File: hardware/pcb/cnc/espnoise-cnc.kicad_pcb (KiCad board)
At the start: 2 copper layers, 70 x 50 mm, 18 parts, among them J1 USB-C 5V JST XH 1x2, J2 CONTROLLER JST XH 1x10, J3 LED STRIP JST XH 1x5, Q1 2N3904, SW1 MUTE (7-7 WS), SW2 BUZZER ENABLE (7-7 ZS), U1 SN74AHCT125N

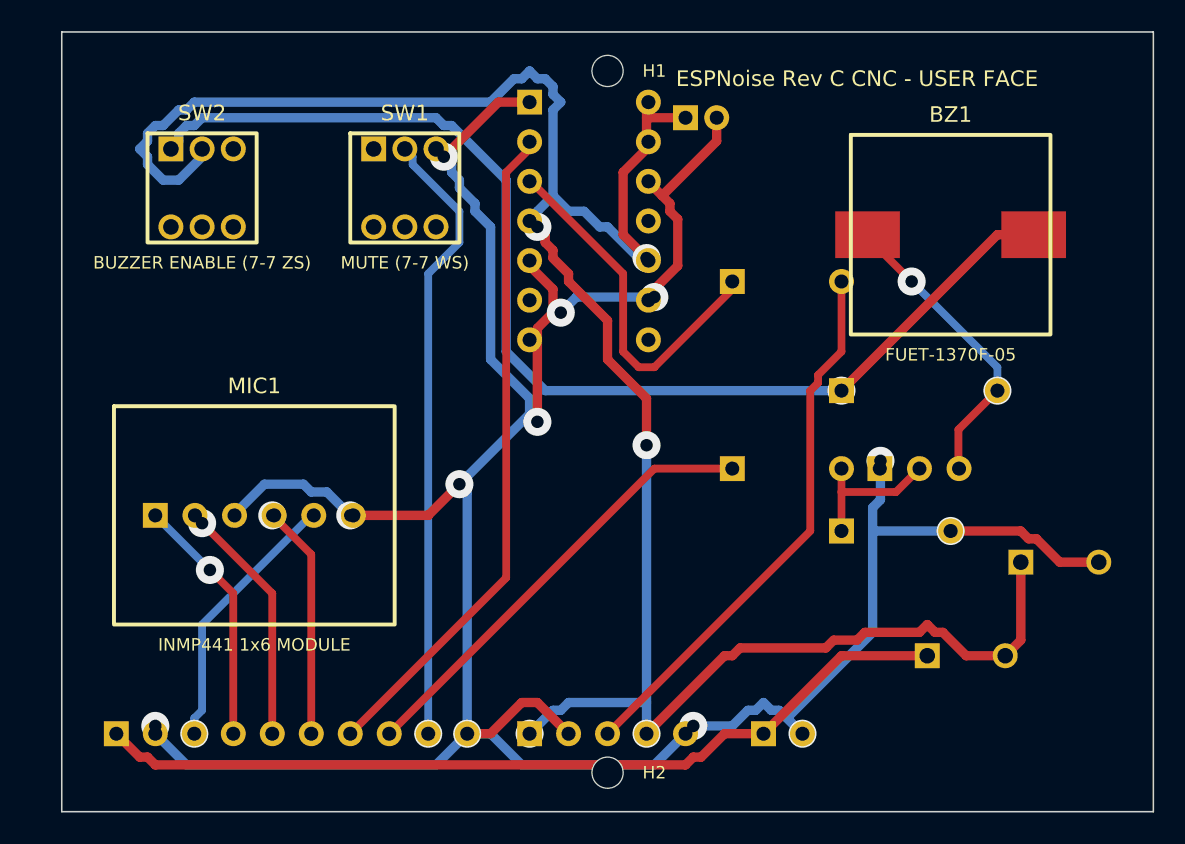
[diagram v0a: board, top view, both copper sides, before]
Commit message: Fit two lean CNC PCBs on one panel
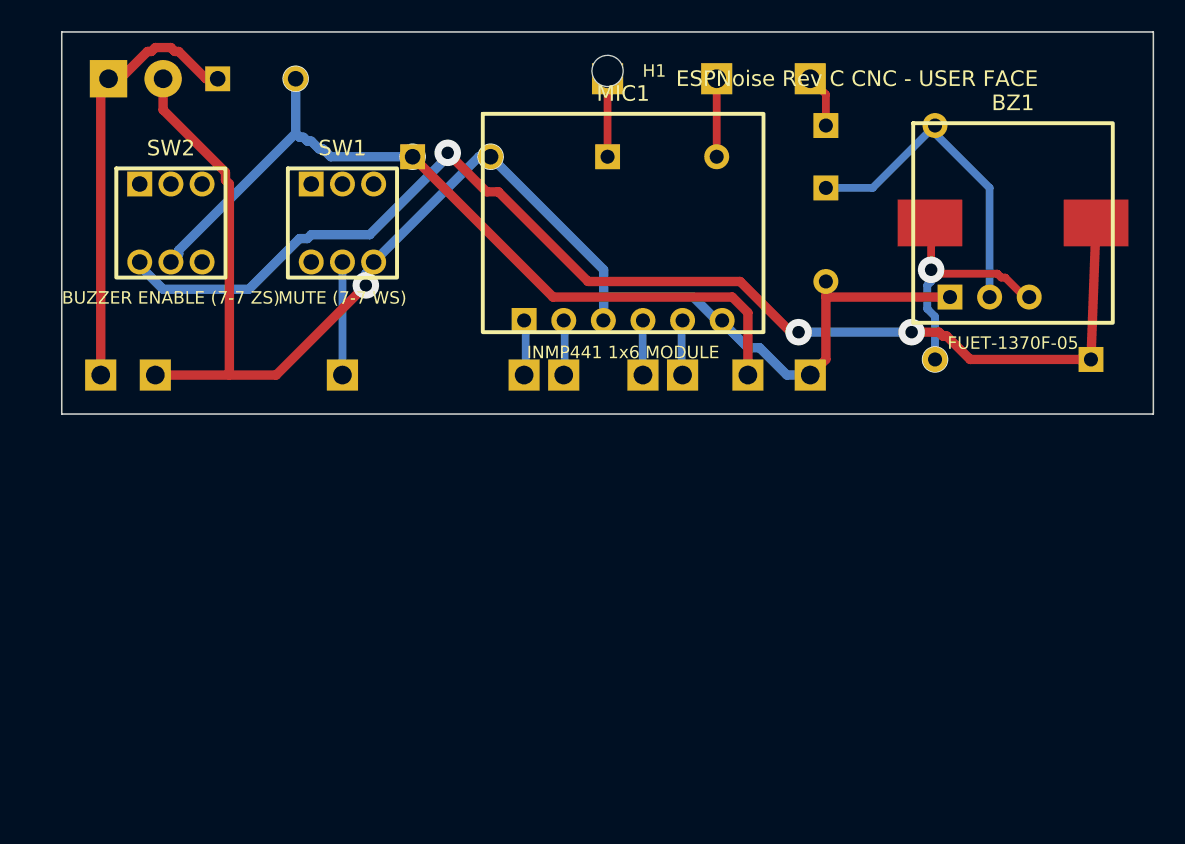
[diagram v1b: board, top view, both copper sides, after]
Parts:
- removed C1: 100nF, THT:C_Disc_P2.00mm
- removed H2: , Mechanical:RegistrationHole_2mm
- removed J1: USB-C 5V JST XH 1x2, JST:B2B-XH-A
- removed J2: CONTROLLER JST XH 1x10, JST:B10B-XH-A
- removed J3: LED STRIP JST XH 1x5, JST:B5B-XH-A
- removed U1: SN74AHCT125N, Package_DIP:DIP-14_W7.62mm
- added P1: 5 V POWER WIRES, ESPNoise:WirePads_2_P3.5mm, B.Cu at (0.00, 0.00)
- added W1: ESP32 +5V, ESPNoise:WireTerminal_D2.0mm, B.Cu at (0.00, 0.00)
- added W10: LED +5V, ESPNoise:WireTerminal_D2.0mm, B.Cu at (0.00, 0.00)
- added W11: LED DATA, ESPNoise:WireTerminal_D2.0mm, B.Cu at (0.00, 0.00)
- added W12: LED GND, ESPNoise:WireTerminal_D2.0mm, B.Cu at (0.00, 0.00)
- added W2: ESP32 GND, ESPNoise:WireTerminal_D2.0mm, B.Cu at (0.00, 0.00)
- added W3: ESP32 MUTE, ESPNoise:WireTerminal_D2.0mm, B.Cu at (0.00, 0.00)
- added W4: ESP32 MIC SCK, ESPNoise:WireTerminal_D2.0mm, B.Cu at (0.00, 0.00)
- added W5: ESP32 MIC WS, ESPNoise:WireTerminal_D2.0mm, B.Cu at (0.00, 0.00)
- added W6: ESP32 MIC SD, ESPNoise:WireTerminal_D2.0mm, B.Cu at (0.00, 0.00)
- added W7: ESP32 3V3, ESPNoise:WireTerminal_D2.0mm, B.Cu at (0.00, 0.00)
- added W8: ESP32 LED DATA, ESPNoise:WireTerminal_D2.0mm, B.Cu at (0.00, 0.00)
- added W9: ESP32 BUZZER, ESPNoise:WireTerminal_D2.0mm, B.Cu at (0.00, 0.00)
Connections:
- R1 pad 1: LED_DATA_5V_RAW -> LED_DATA_3V3
- R1 pad 2: LED_DATA_5V -> LED_DATA
- SW1 pad 2: MUTE_N -> (no net)
- SW1 pad 3: GND -> (no net)
- SW1 pad 5: (no net) -> MUTE_N
- SW1 pad 6: (no net) -> GND
- SW2 pad 1: +5V_BUZZER_SW -> (no net)
- SW2 pad 2: +5V_PERIPH -> (no net)
- SW2 pad 4: (no net) -> +5V_BUZZER_SW
- SW2 pad 5: (no net) -> +5V_PERIPH
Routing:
- net GND: track 192.7 -> 91.9 mm, vias 12 -> 3
- net +5V_PERIPH: track 144.3 -> 52.8 mm, vias 5 -> 2
- net LED_DATA_3V3: track 42.8 -> 5.00 mm
- net LED_DATA_5V: track 35.2 -> 0.00 mm
- net MUTE_N: track 39.8 -> 7.25 mm
- net +5V_IN: track 55.7 -> 27.9 mm
- net BUZZER_PWM: track 29.0 -> 3.41 mm
- net LED_DATA_5V_RAW: track 23.5 -> 0.00 mm
- net +3V3: track 17.1 -> 3.50 mm
- net MIC_WS: track 16.1 -> 3.50 mm
- net MIC_SCK: track 16.1 -> 3.50 mm
- net MIC_SD: track 15.0 -> 3.50 mm
- net BUZZER_BASE: track 9.62 -> 21.0 mm
- net +5V_BUZZER_SW: track 74.5 -> 79.9 mm, vias 1 -> 3
- net LED_DATA: track 0.00 -> 5.00 mm
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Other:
- board size 70 x 50 mm -> 70 x 24.5 mm
- board text added: "INTERNAL - SOLDER WIRE VIAS BOTH FACES"
- board text removed: "INTERNAL FACE - WIRE VIAS: SOLDER BOTH FACES"

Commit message: Correct CNC microphone and buzzer footprints
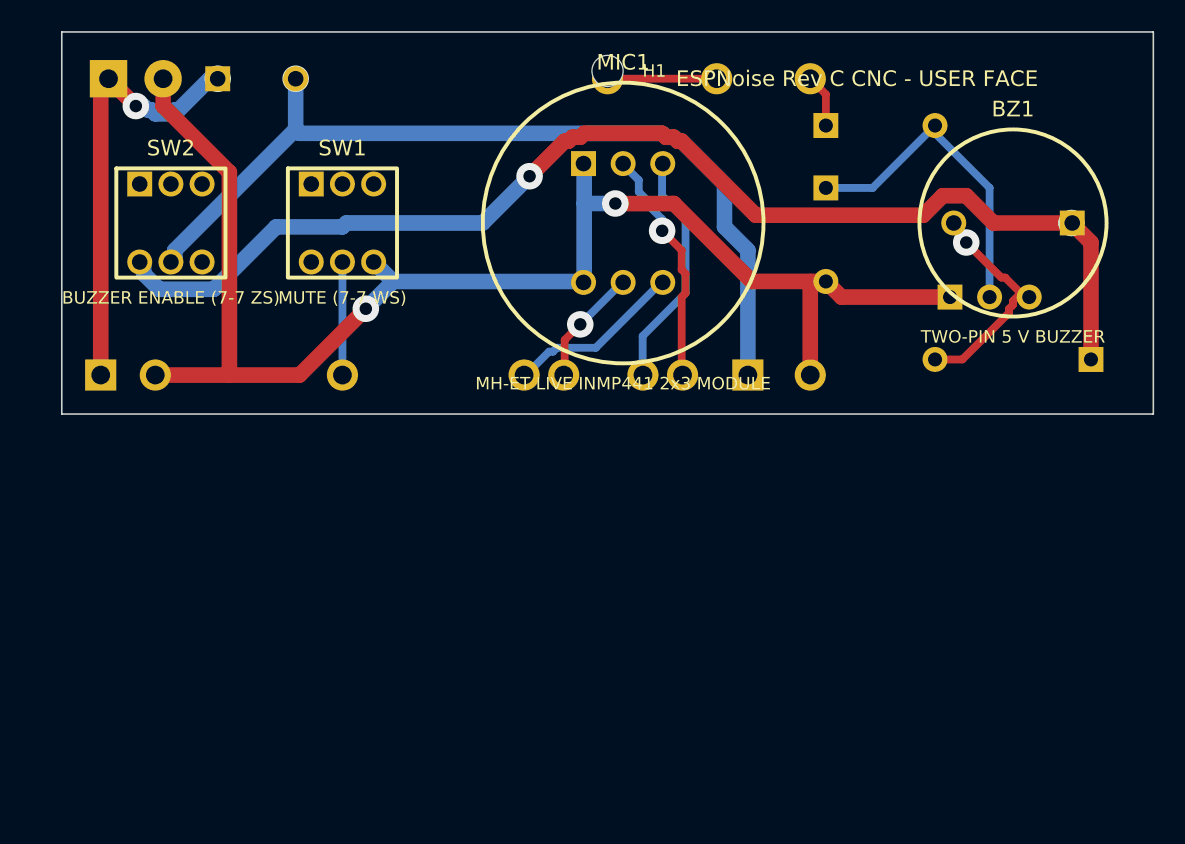
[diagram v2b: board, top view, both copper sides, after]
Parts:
- removed C2: 1000uF 10V, THT:CP_Radial_D8_P5.00mm
- removed P1: 5 V POWER WIRES, ESPNoise:WirePads_2_P3.5mm
- removed R1: 330R, THT:Axial
- removed W1: ESP32 +5V, ESPNoise:WireTerminal_D2.0mm
- removed W10: LED +5V, ESPNoise:WireTerminal_D2.0mm
- removed W11: LED DATA, ESPNoise:WireTerminal_D2.0mm
- removed W12: LED GND, ESPNoise:WireTerminal_D2.0mm
- removed W2: ESP32 GND, ESPNoise:WireTerminal_D2.0mm
- removed W3: ESP32 MUTE, ESPNoise:WireTerminal_D2.0mm
- removed W4: ESP32 MIC SCK, ESPNoise:WireTerminal_D2.0mm
- removed W5: ESP32 MIC WS, ESPNoise:WireTerminal_D2.0mm
- removed W6: ESP32 MIC SD, ESPNoise:WireTerminal_D2.0mm
- removed W7: ESP32 3V3, ESPNoise:WireTerminal_D2.0mm
- removed W8: ESP32 LED DATA, ESPNoise:WireTerminal_D2.0mm
- removed W9: ESP32 BUZZER, ESPNoise:WireTerminal_D2.0mm
- added J_ESP32: ESP32 INDIVIDUAL WIRES, ESPNoise:IndividualWireGroup_ESP32, B.Cu at (0.00, 0.00)
- added J_LED: LED STRIP INDIVIDUAL WIRES, ESPNoise:IndividualWireGroup_LED, B.Cu at (0.00, 0.00)
- added PWR1: 5 V POWER WIRES, ESPNoise:WirePads_2_P3.5mm, B.Cu at (0.00, 0.00)
- BZ1: value FUET-1370F-05 -> TWO-PIN 5 V BUZZER; footprint ESPNoise:FUET-1370F-05 -> ESPNoise:Buzzer_THT_2Pin_P7.60mm_D12mm
- MIC1: value INMP441 1x6 MODULE -> MH-ET LIVE INMP441 2x3 MODULE; footprint ESPNoise:INMP441_1x6_P2.54mm -> ESPNoise:MH_ET_LIVE_INMP441_2x3_P2.54_Row7.62
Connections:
- MIC1 pad 1: MIC_SCK -> GND
- MIC1 pad 2: MIC_WS -> +3V3
- MIC1 pad 3: GND -> MIC_SD
- MIC1 pad 4: MIC_SD -> GND
- MIC1 pad 5: +3V3 -> MIC_WS
- MIC1 pad 6: GND -> MIC_SCK
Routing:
- net +3V3: track 3.50 -> 15.3 mm
- net MIC_SD: track 3.50 -> 15.3 mm
- net MIC_SCK: track 3.50 -> 11.2 mm
- net LED_DATA_3V3: track 5.00 -> 0.00 mm
- net +5V_PERIPH: track 52.8 -> 56.9 mm
- net MIC_WS: track 3.50 -> 7.55 mm
- net +5V_BUZZER_SW: track 79.9 -> 77.6 mm, vias 3 -> 2
- net LED_DATA: track 5.00 -> 7.00 mm
- net BUZZER_COLLECTOR: track 16.0 -> 14.6 mm, vias 2 -> 1
- net +5V_IN: track 27.9 -> 28.1 mm, vias 0 -> 2
- net GND: track 91.9 -> 92.0 mm, vias 3 -> 2

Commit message: Apply measured CNC part dimensions
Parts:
- BZ1: footprint ESPNoise:Buzzer_THT_2Pin_P7.60mm_D12mm -> ESPNoise:Buzzer_THT_2Pin_P6.50mm_D12mm
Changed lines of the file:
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@@
     (layer "F.Cu")
     (at 0 0)
-    (property "Reference" "MIC1" (at 36.000 1.950 0) (layer "F.SilkS") (effects (font (size 1 1) (thickness 0.15))))
-    (property "Value" "MH-ET LIVE INMP441 2x3 MODULE" (at 36.000 22.550 0) (layer "F.SilkS") (effects (font (size 0.8 0.8) (thickness 0.12))))
-    (fp_circle (center 36.000 12.250) (end 45.000 12.250) (stroke (width 0.25) (type default)) (fill none) (layer "F.SilkS"))
+    (property "Reference" "MIC1" (at 36.000 4.450 0) (layer "F.SilkS") (effects (font (size 1 1) (thickness 0.15))))
+    (property "Value" "MH-ET LIVE INMP441 2x3 MODULE" (at 36.000 20.050 0) (layer "F.SilkS") (effects (font (size 0.8 0.8) (thickness 0.12))))
+    (fp_circle (center 36.000 12.250) (end 42.500 12.250) (stroke (width 0.25) (type default)) (fill none) (layer "F.SilkS"))
     (pad "1" thru_hole rect (at 33.460 8.440) (size 1.600 1.600) (drill 1.000) (layers "*.Cu" "*.Mask") (net 8 "GND"))
     (pad "2" thru_hole circle (at 36.000 8.440) (size 1.600 1.600) (drill 1.000) (layers "*.Cu" "*.Mask") (net 1 "+3V3"))
@@
     (pad "6" thru_hole circle (at 38.540 16.060) (size 1.600 1.600) (drill 1.000) (layers "*.Cu" "*.Mask") (net 10 "MIC_SCK"))
   )
-  (footprint "ESPNoise:Buzzer_THT_2Pin_P7.60mm_D12mm"
+  (footprint "ESPNoise:Buzzer_THT_2Pin_P6.50mm_D12mm"
     (layer "F.Cu")
     (at 0 0)
@@
     (property "Value" "TWO-PIN 5 V BUZZER" (at 61.000 19.550 0) (layer "F.SilkS") (effects (font (size 0.8 0.8) (thickness 0.12))))
     (fp_circle (center 61.000 12.250) (end 67.000 12.250) (stroke (width 0.25) (type default)) (fill none) (layer "F.SilkS"))
-    (pad "1" thru_hole rect (at 64.800 12.250) (size 1.600 1.600) (drill 1.000) (layers "*.Cu" "*.Mask") (net 2 "+5V_BUZZER_SW"))
-    (pad "2" thru_hole circle (at 57.200 12.250) (size 1.600 1.600) (drill 1.000) (layers "*.Cu" "*.Mask") (net 6 "BUZZER_COLLECTOR"))
+    (pad "1" thru_hole rect (at 64.250 12.250) (size 1.600 1.600) (drill 0.800) (layers "*.Cu" "*.Mask") (net 2 "+5V_BUZZER_SW"))
+    (pad "2" thru_hole circle (at 57.750 12.250) (size 1.600 1.600) (drill 0.800) (layers "*.Cu" "*.Mask") (net 6 "BUZZER_COLLECTOR"))
   )
   (footprint "ESPNoise:WirePads_2_P3.5mm"
@@
   (segment (start 55.750 6.250) (end 59.500 10.000) (width 0.500) (layer "B.Cu") (net 5))
   (segment (start 59.500 10.000) (end 59.500 17.000) (width 0.500) (layer "B.Cu") (net 5))
-  (segment (start 57.250 12.250) (end 57.500 12.500) (width 0.500) (layer "B.Cu") (net 6))
-  (segment (start 57.500 12.500) (end 57.500 12.750) (width 0.500) (layer "B.Cu") (net 6))
-  (segment (start 57.500 12.750) (end 57.750 13.000) (width 0.500) (layer "B.Cu") (net 6))
-  (segment (start 57.750 13.000) (end 57.750 13.250) (width 0.500) (layer "B.Cu") (net 6))
-  (segment (start 57.750 13.250) (end 58.000 13.500) (width 0.500) (layer "B.Cu") (net 6))
-  (segment (start 58.000 13.500) (end 60.250 15.750) (width 0.500) (layer "F.Cu") (net 6))
-  (segment (start 60.250 15.750) (end 60.500 15.750) (width 0.500) (layer "F.Cu") (net 6))
-  (segment (start 60.500 15.750) (end 61.750 17.000) (width 0.500) (layer "F.Cu") (net 6))
-  (segment (start 61.750 17.000) (end 62.000 17.000) (width 0.500) (layer "F.Cu") (net 6))
-  (segment (start 61.500 16.750) (end 61.000 17.250) (width 0.500) (layer "F.Cu") (net 6))
-  (segment (start 61.000 17.250) (end 61.000 17.500) (width 0.500) (layer "F.Cu") (net 6))
-  (segment (start 61.000 17.500) (end 60.750 17.750) (width 0.500) (layer "F.Cu") (net 6))
-  (segment (start 60.750 17.750) (end 60.750 18.000) (width 0.500) (layer "F.Cu") (net 6))
-  (segment (start 60.750 18.000) (end 57.750 21.000) (width 0.500) (layer "F.Cu") (net 6))
-  (segment (start 57.750 21.000) (end 56.000 21.000) (width 0.500) (layer "F.Cu") (net 6))
+  (segment (start 57.750 12.250) (end 58.000 12.500) (width 0.500) (layer "B.Cu") (net 6))
+  (segment (start 58.000 12.500) (end 62.000 16.500) (width 0.500) (layer "F.Cu") (net 6))
+  (segment (start 62.000 16.500) (end 62.000 17.000) (width 0.500) (layer "F.Cu") (net 6))
+  (segment (start 62.000 17.000) (end 58.000 21.000) (width 0.500) (layer "F.Cu") (net 6))
+  (segment (start 58.000 21.000) (end 56.000 21.000) (width 0.500) (layer "F.Cu") (net 6))
   (segment (start 5.000 14.750) (end 5.250 15.000) (width 1.000) (layer "B.Cu") (net 2))
   (segment (start 5.250 15.000) (end 5.250 15.500) (width 1.000) (layer "B.Cu") (net 2))
@@
   (segment (start 39.500 7.000) (end 39.750 7.000) (width 1.000) (layer "F.Cu") (net 2))
   (segment (start 39.750 7.000) (end 44.500 11.750) (width 1.000) (layer "F.Cu") (net 2))
-  (segment (start 44.500 11.750) (end 55.250 11.750) (width 1.000) (layer "F.Cu") (net 2))
-  (segment (start 55.250 11.750) (end 56.500 10.500) (width 1.000) (layer "F.Cu") (net 2))
-  (segment (start 56.500 10.500) (end 58.000 10.500) (width 1.000) (layer "F.Cu") (net 2))
-  (segment (start 58.000 10.500) (end 59.750 12.250) (width 1.000) (layer "F.Cu") (net 2))
-  (segment (start 59.750 12.250) (end 64.750 12.250) (width 1.000) (layer "F.Cu") (net 2))
-  (segment (start 64.750 12.250) (end 66.000 13.500) (width 1.000) (layer "F.Cu") (net 2))
-  (segment (start 66.000 13.500) (end 66.000 21.000) (width 1.000) (layer "F.Cu") (net 2))
+  (segment (start 44.500 11.750) (end 55.750 11.750) (width 1.000) (layer "F.Cu") (net 2))
+  (segment (start 55.750 11.750) (end 57.000 10.500) (width 1.000) (layer "F.Cu") (net 2))
+  (segment (start 57.000 10.500) (end 58.500 10.500) (width 1.000) (layer "F.Cu") (net 2))
+  (segment (start 58.500 10.500) (end 60.250 12.250) (width 1.000) (layer "F.Cu") (net 2))
+  (segment (start 60.250 12.250) (end 64.250 12.250) (width 1.000) (layer "F.Cu") (net 2))
+  (segment (start 64.250 12.250) (end 66.000 14.000) (width 1.000) (layer "F.Cu") (net 2))
+  (segment (start 66.000 14.000) (end 66.000 21.000) (width 1.000) (layer "F.Cu") (net 2))
   (via (at 29.750 22.000) (size 1.700) (drill 0.800) (layers "F.Cu" "B.Cu") (net 10))
   (via (at 33.250 18.750) (size 1.700) (drill 0.800) (layers "F.Cu" "B.Cu") (net 12))
@@
   (via (at 15.000 3.000) (size 1.700) (drill 0.800) (layers "F.Cu" "B.Cu") (net 4))
   (via (at 44.000 22.000) (size 1.700) (drill 0.800) (layers "F.Cu" "B.Cu") (net 4))
-  (via (at 58.000 13.500) (size 1.700) (drill 0.800) (layers "F.Cu" "B.Cu") (net 6))
+  (via (at 58.000 12.500) (size 1.700) (drill 0.800) (layers "F.Cu" "B.Cu") (net 6))
   (via (at 30.000 9.250) (size 1.700) (drill 0.800) (layers "F.Cu" "B.Cu") (net 2))
-  (via (at 64.750 12.250) (size 1.700) (drill 0.800) (layers "F.Cu" "B.Cu") (net 2))
+  (via (at 64.250 12.250) (size 1.700) (drill 0.800) (layers "F.Cu" "B.Cu") (net 2))
   (gr_rect (start 0 0) (end 70.000 24.500) (stroke (width 0.1) (type default)) (fill none) (layer "Edge.Cuts"))
   (gr_text "ESPNoise Rev C CNC - USER FACE" (at 51 3) (layer "F.SilkS") (effects (font (size 1 1) (thickness 0.15))))

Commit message: feat(cnc): widen PCB tracks and user pads
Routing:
- net GND: track 92.0 -> 92.7 mm
